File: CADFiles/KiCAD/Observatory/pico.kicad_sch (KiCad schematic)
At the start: 1 part, among them U5 Pico

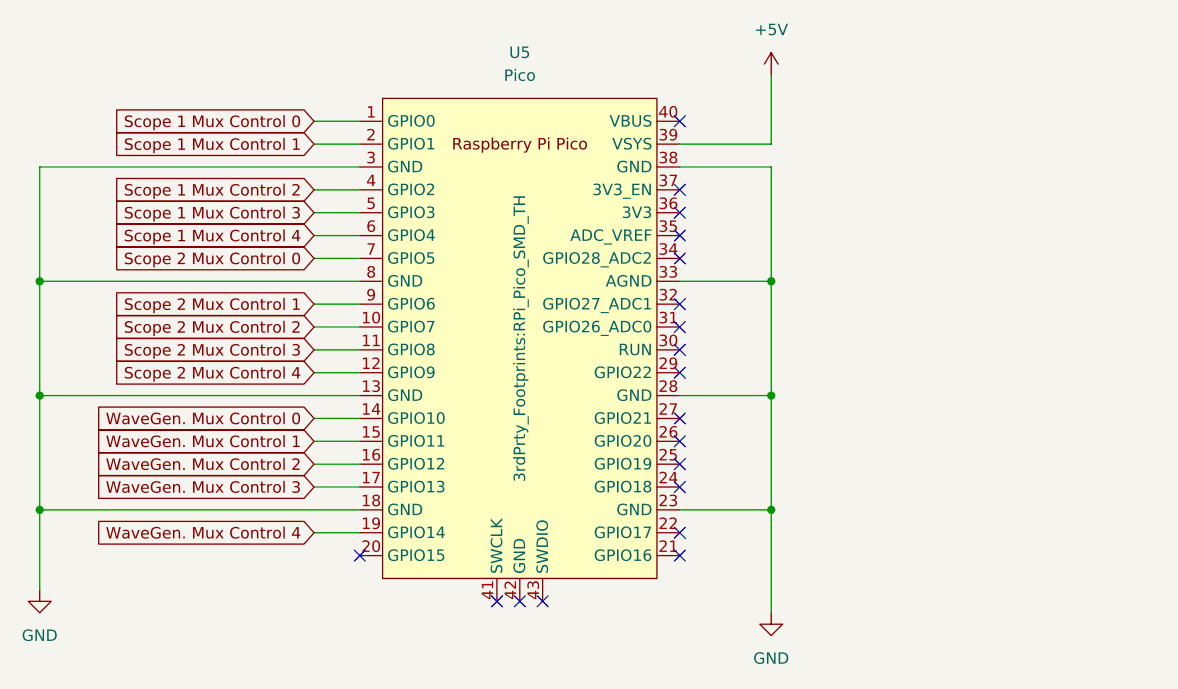
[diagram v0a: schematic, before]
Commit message: All nets routed.
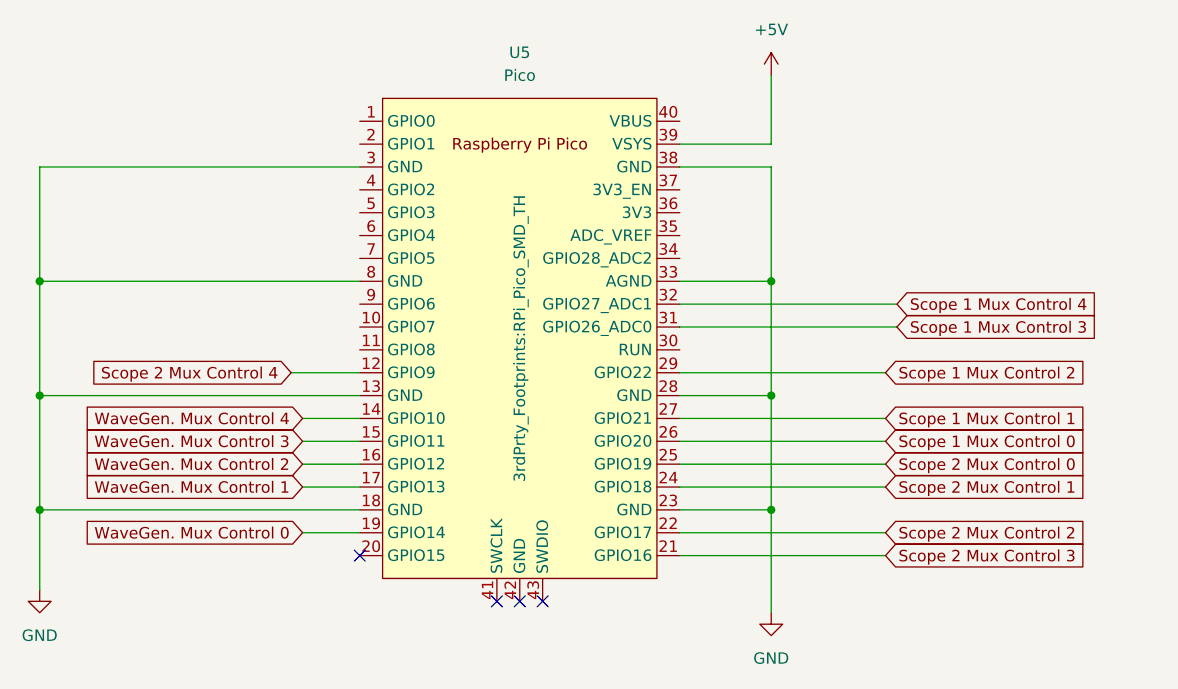
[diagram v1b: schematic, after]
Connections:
- net Scope 1 Mux Control 0: now also U5.26 (GPIO20); no longer U5.1 (GPIO0)
- net Scope 1 Mux Control 1: now also U5.27 (GPIO21); no longer U5.2 (GPIO1)
- net Scope 1 Mux Control 2: now also U5.29 (GPIO22); no longer U5.4 (GPIO2)
- net Scope 1 Mux Control 3: now also U5.31 (GPIO26_ADC0); no longer U5.5 (GPIO3)
- net Scope 1 Mux Control 4: now also U5.32 (GPIO27_ADC1); no longer U5.6 (GPIO4)
- net Scope 2 Mux Control 0: now also U5.25 (GPIO19); no longer U5.7 (GPIO5)
- net Scope 2 Mux Control 1: now also U5.24 (GPIO18); no longer U5.9 (GPIO6)
- net Scope 2 Mux Control 2: now also U5.22 (GPIO17); no longer U5.10 (GPIO7)
- net Scope 2 Mux Control 3: now also U5.21 (GPIO16); no longer U5.11 (GPIO8)
- net WaveGen. Mux Control 0: now also U5.19 (GPIO14); no longer U5.14 (GPIO10)
- net WaveGen. Mux Control 1: now also U5.17 (GPIO13); no longer U5.15 (GPIO11)
- net WaveGen. Mux Control 3: now also U5.15 (GPIO11); no longer U5.17 (GPIO13)
- net WaveGen. Mux Control 4: now also U5.14 (GPIO10); no longer U5.19 (GPIO14)
- no-connect marks 19 -> 4

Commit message: AD DC(-) error fixed. Jumpers added for feet grounds and DC supplies
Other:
- company: (none) -> West Lab
- title: (none) -> SCuM Observatory
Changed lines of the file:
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@@
 	(generator_version "9.0")
 	(paper "A4")
+	(title_block
+		(title "SCuM Observatory")
+		(date "2025-03-21")
+		(rev "2")
+		(company "West Lab")
+	)
 	(junction
 		(at 154.94 128.27)

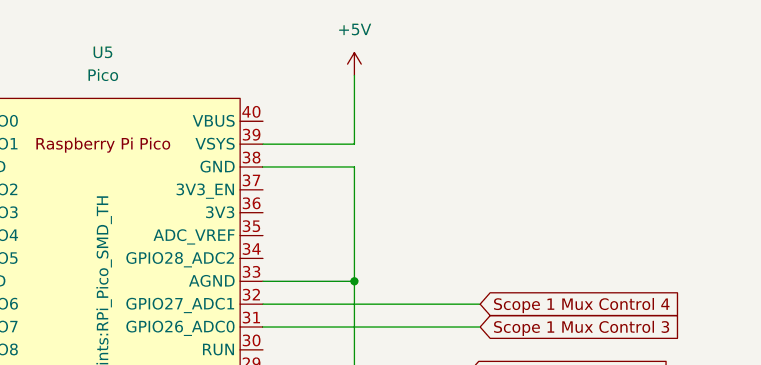
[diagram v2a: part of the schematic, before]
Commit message: Fixs: Disconnnect pico Vsys from board. RX/TX pin errors, 3WD_CLK pin.
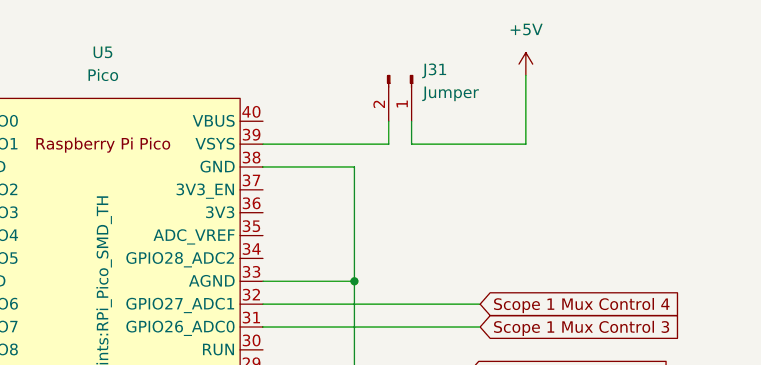
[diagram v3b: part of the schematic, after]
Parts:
- added J31: Jumper, Jumper:SolderJumper-2_P1.3mm_Open_Pad1.0x1.5mm, symbol Connector:Conn_01x02_Pin
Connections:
- net +5V: now also J31.1 (Pin_1); no longer U5.39 (VSYS)
- new net: J31.2 (Pin_2), U5.39 (VSYS)
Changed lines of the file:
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@@
 	(wire
 		(pts
-			(xy 144.78 87.63) (xy 154.94 87.63)
-		)
-		(stroke
-			(width 0)
-			(type default)
-		)
-	)
-	(wire
-		(pts
-			(xy 154.94 80.01) (xy 154.94 87.63)
+			(xy 161.29 87.63) (xy 173.99 87.63)
+		)
+		(stroke
+			(width 0)
+			(type default)
+		)
+	)
+	(wire
+		(pts
+			(xy 144.78 87.63) (xy 158.75 87.63)
 		)
 		(stroke
@@
 	(wire
 		(pts
+			(xy 158.75 87.63) (xy 158.75 85.09)
+		)
+		(stroke
+			(width 0)
+			(type default)
+		)
+	)
+	(wire
+		(pts
 			(xy 101.6 113.03) (xy 109.22 113.03)
 		)
@@
 	(wire
 		(pts
+			(xy 173.99 87.63) (xy 173.99 80.01)
+		)
+		(stroke
+			(width 0)
+			(type default)
+		)
+	)
+	(wire
+		(pts
 			(xy 144.78 115.57) (xy 154.94 115.57)
 		)
@@
 		(pts
 			(xy 102.87 120.65) (xy 109.22 120.65)
+		)
+		(stroke
+			(width 0)
+			(type default)
+		)
+	)
+	(wire
+		(pts
+			(xy 161.29 87.63) (xy 161.29 85.09)
 		)
 		(stroke
@@
 	(symbol
 		(lib_id "power:+5V")
-		(at 154.94 80.01 0)
+		(at 173.99 80.01 0)
 		(unit 1)
 		(exclude_from_sim no)
@@
 		(fields_autoplaced yes)
 		(property "Reference" "#PWR036"
-			(at 154.94 83.82 0)
+			(at 173.99 83.82 0)
 			(effects
 				(font
@@
 		)
 		(property "Value" "+5V"
-			(at 154.94 74.93 0)
+			(at 173.99 74.93 0)
 			(effects
 				(font
@@
 		)
 		(property "Footprint" ""
-			(at 154.94 80.01 0)
+			(at 173.99 80.01 0)
 			(effects
 				(font
@@
 		)
 		(property "Datasheet" ""
-			(at 154.94 80.01 0)
+			(at 173.99 80.01 0)
 			(effects
 				(font
@@
 		)
 		(property "Description" "Power symbol creates a global label with name \"+5V\""
-			(at 154.94 80.01 0)
+			(at 173.99 80.01 0)
 			(effects
 				(font
@@
 					(unit 1)
 				)
+			)
+		)
+	)
+	(symbol
+		(lib_id "Connector:Conn_01x02_Pin")
+		(at 161.29 80.01 270)
+		(unit 1)
+		(exclude_from_sim no)
+		(in_bom yes)
+		(on_board yes)
+		(dnp no)
+		(fields_autoplaced yes)
+		(property "Reference" "J31"
+			(at 162.56 79.3749 90)
+			(effects
+				(font
+					(size 1.27 1.27)
+				)
+				(justify left)
+			)
+		)
+		(property "Value" "Jumper"
+			(at 162.56 81.9149 90)
+			(effects
+				(font
+					(size 1.27 1.27)
+				)
+				(justify left)
+			)
+		)
+		(property "Footprint" "Jumper:SolderJumper-2_P1.3mm_Open_Pad1.0x1.5mm"
+			(at 161.29 80.01 0)
+			(effects
+				(font
+					(size 1.27 1.27)
+				)
+				(hide yes)
+			)
+		)
+		(property "Datasheet" "~"
+			(at 161.29 80.01 0)
+			(effects
+				(font
+					(size 1.27 1.27)
+				)
+				(hide yes)
+			)
+		)
+		(property "Description" "Generic connector, single row, 01x02, script generated"
+			(at 161.29 80.01 0)
+			(effects
+				(font
+					(size 1.27 1.27)
+				)
+				(hide yes)
+			)
+		)
+		(pin "1"
+		)
+		(pin "2"
+		)
+		(instances
+			(project "Observatory"
+				(path "/70f40ce9-32c8-42da-85f6-43c2f6e1fb63/425e7d77-b9d1-4360-8c64-8325327d8c9f"
+					(reference "J31")
+					(unit 1)
+				)
